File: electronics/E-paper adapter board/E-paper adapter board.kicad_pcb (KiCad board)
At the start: 2 copper layers, 50.8 x 49.7 mm, 9 parts, among them J1 EXTRA, J2 SWD, J3 J-LINK, J4 nRF-PPK2, J5 DEBUG

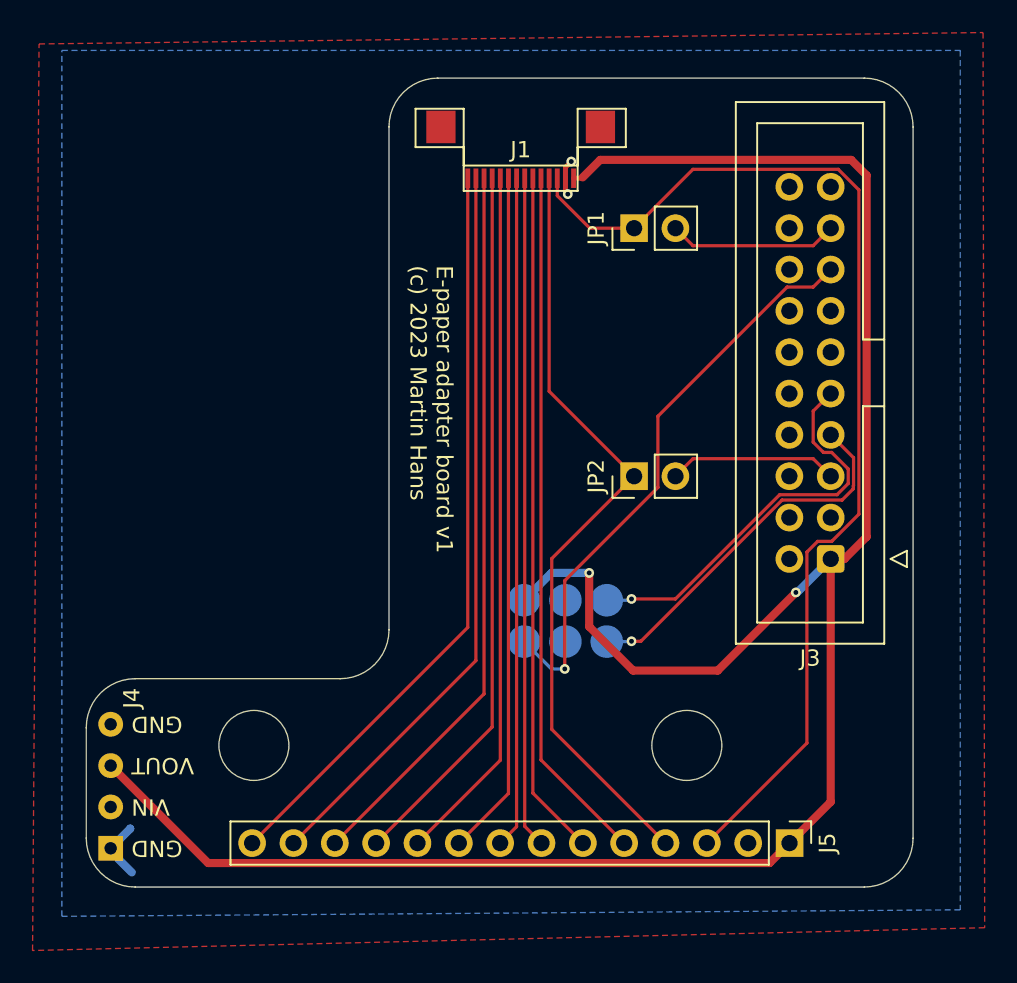
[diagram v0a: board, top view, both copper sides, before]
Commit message: fix TP4056 footprint
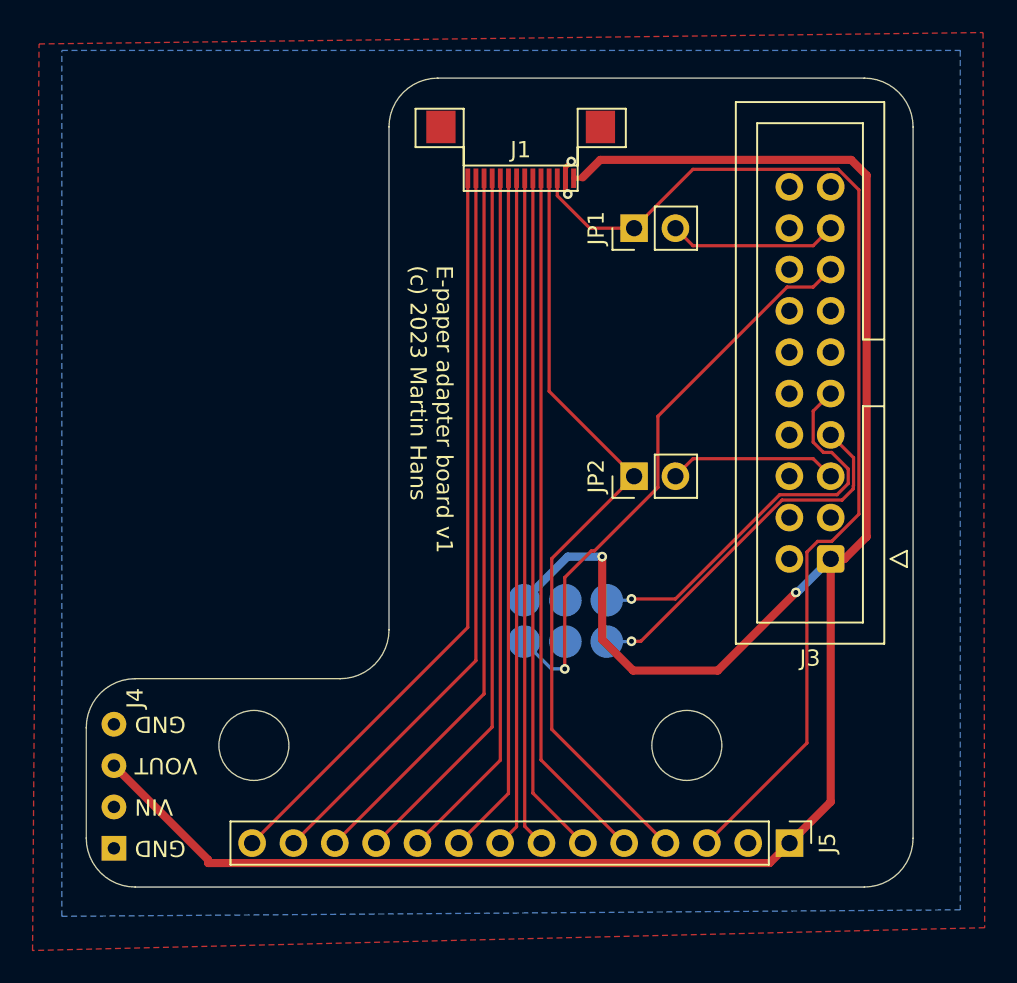
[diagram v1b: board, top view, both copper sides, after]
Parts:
- moved J4 0.20 mm to (114.5, 147.3)
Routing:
- net GND: track 5.95 -> 2.39 mm
- net +3V0: track 133.8 -> 135.6 mm
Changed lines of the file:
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@@
     (property "ki_description" "Mounting Hole without connection")
     (property "ki_keywords" "mounting hole")
-    (attr exclude_from_pos_files)
+    (attr exclude_from_pos_files exclude_from_bom)
     (fp_text reference "H2" (at 0 -4.75) (layer "F.SilkS") hide
         (effects (font (size 1 1) (thickness 0.15)))
@@
   )
   (footprint "project:nRF-PPK2_power" (layer "F.Cu")
-    (at 114.3 147.32 90)
+    (at 114.5 147.32 90)
     (property "Config" "+ci")
     (property "LCSC" "C2897386")
@@
     (property "ki_description" "Mounting Hole without connection")
     (property "ki_keywords" "mounting hole")
-    (attr exclude_from_pos_files)
+    (attr exclude_from_pos_files exclude_from_bom)
     (fp_text reference "H1" (at 0 -4.75) (layer "F.SilkS") hide
         (effects (font (size 1 1) (thickness 0.15)))
@@
     (property "ki_description" "Generic connector, double row, 02x03, counter clockwise pin numbering scheme (similar to DIP package numbering), script generated (kicad-library-utils/schlib/autogen/connector/)")
     (property "ki_keywords" "connector")
-    (attr smd exclude_from_bom)
+    (attr smd exclude_from_pos_files exclude_from_bom)
     (fp_text reference "J2" (at 0 3.81 unlocked) (layer "B.SilkS")
         (effects (font (size 1 1) (thickness 0.15)) (justify mirror))
@@
   )
   (segment (start 142.74 106.15) (end 143.25 106.15) (width 0.3) (layer "F.Cu") (net 1))
-  (segment (start 143.7 133.7) (end 146.4 136.4) (width 0.5) (layer "F.Cu") (net 1))
   (segment (start 120.287 148.227) (end 154.783 148.227) (width 0.5) (layer "F.Cu") (net 1))
+  (segment (start 120.287 148.027) (end 114.5 142.24) (width 0.5) (layer "F.Cu") (net 1))
+  (segment (start 146.4 136.4) (end 144.5 134.5) (width 0.5) (layer "F.Cu") (net 1))
   (segment (start 160.748 105.97342) (end 160.748 128.182) (width 0.5) (layer "F.Cu") (net 1))
   (segment (start 144.377 105.023) (end 159.79758 105.023) (width 0.5) (layer "F.Cu") (net 1))
-  (segment (start 146.4 136.4) (end 151.6 136.4) (width 0.5) (layer "F.Cu") (net 1))
   (segment (start 158.54 144.47) (end 156.01 147) (width 0.5) (layer "F.Cu") (net 1))
-  (segment (start 151.6 136.4) (end 156.4 131.6) (width 0.5) (layer "F.Cu") (net 1))
   (segment (start 143.25 106.15) (end 143.3 106.1) (width 0.3) (layer "F.Cu") (net 1))
   (segment (start 160.748 128.182) (end 159.39 129.54) (width 0.5) (layer "F.Cu") (net 1))
   (segment (start 159.39 129.54) (end 158.54 129.54) (width 0.5) (layer "F.Cu") (net 1))
-  (segment (start 114.3 142.24) (end 120.287 148.227) (width 0.5) (layer "F.Cu") (net 1))
-  (segment (start 143.7 130.4) (end 143.7 133.7) (width 0.5) (layer "F.Cu") (net 1))
+  (segment (start 156.4 131.6) (end 151.6 136.4) (width 0.5) (layer "F.Cu") (net 1))
   (segment (start 159.79758 105.023) (end 160.748 105.97342) (width 0.5) (layer "F.Cu") (net 1))
   (segment (start 143.3 106.1) (end 144.377 105.023) (width 0.5) (layer "F.Cu") (net 1))
   (segment (start 158.54 129.54) (end 158.54 144.47) (width 0.5) (layer "F.Cu") (net 1))
+  (segment (start 120.287 148.227) (end 120.287 148.027) (width 0.5) (layer "F.Cu") (net 1))
+  (segment (start 144.5 134.5) (end 144.5 129.4) (width 0.5) (layer "F.Cu") (net 1))
+  (segment (start 151.6 136.4) (end 146.4 136.4) (width 0.5) (layer "F.Cu") (net 1))
   (segment (start 154.783 148.227) (end 156.01 147) (width 0.5) (layer "F.Cu") (net 1))
   (via (at 156.4 131.6) (size 0.6) (drill 0.3) (layers "F.Cu" "B.Cu") (net 1))
-  (via (at 143.7 130.4) (size 0.6) (drill 0.3) (layers "F.Cu" "B.Cu") (net 1))
-  (segment (start 141.38 130.4) (end 143.7 130.4) (width 0.5) (layer "B.Cu") (net 1))
+  (via (at 144.5 129.4) (size 0.6) (drill 0.3) (layers "F.Cu" "B.Cu") (net 1))
   (segment (start 156.48 131.6) (end 158.54 129.54) (width 0.5) (layer "B.Cu") (net 1))
-  (segment (start 139.7 132.08) (end 141.38 130.4) (width 0.5) (layer "B.Cu") (net 1))
+  (segment (start 139.7 132.08) (end 142.38 129.4) (width 0.5) (layer "B.Cu") (net 1))
+  (segment (start 142.38 129.4) (end 144.5 129.4) (width 0.5) (layer "B.Cu") (net 1))
   (segment (start 156.4 131.6) (end 156.48 131.6) (width 0.5) (layer "B.Cu") (net 1))
   (segment (start 142.24 105.483498) (end 142.6 105.123498) (width 0.3) (layer "F.Cu") (net 2))
@@
   (via (at 142.38652 107.124832) (size 0.6) (drill 0.3) (layers "F.Cu" "B.Cu") (net 2))
   (via (at 142.6 105.123498) (size 0.6) (drill 0.3) (layers "F.Cu" "B.Cu") (net 2))
-  (segment (start 114.3 147.5) (end 115.6 148.8) (width 0.5) (layer "B.Cu") (net 2))
   (segment (start 114.3 147.32) (end 114.3 147.5) (width 0.5) (layer "B.Cu") (net 2))
-  (segment (start 115.5 146.1) (end 115.5 146.12) (width 0.5) (layer "B.Cu") (net 2))
-  (segment (start 114.3 147.32) (end 115.5 146.12) (width 0.5) (layer "B.Cu") (net 2))
   (segment (start 157.077 140.853) (end 150.93 147) (width 0.2) (layer "F.Cu") (net 3))
   (segment (start 146.46 109.22) (end 150.077 105.603) (width 0.2) (layer "F.Cu") (net 3))
@@
   (segment (start 146.28 134.62) (end 146.3 134.6) (width 0.2) (layer "B.Cu") (net 16))
   (segment (start 147.923 120.777) (end 155.863 112.837) (width 0.2) (layer "F.Cu") (net 18))
-  (segment (start 142.2 130.874) (end 147.923 125.151) (width 0.2) (layer "F.Cu") (net 18))
+  (segment (start 143.830761 129.05) (end 144.024 129.05) (width 0.2) (layer "F.Cu") (net 18))
   (segment (start 147.923 125.151) (end 147.923 120.777) (width 0.2) (layer "F.Cu") (net 18))
-  (segment (start 142.2 136.3) (end 142.2 130.874) (width 0.2) (layer "F.Cu") (net 18))
+  (segment (start 144.024 129.05) (end 147.923 125.151) (width 0.2) (layer "F.Cu") (net 18))
+  (segment (start 142.2 136.3) (end 142.2 130.680761) (width 0.2) (layer "F.Cu") (net 18))
+  (segment (start 142.2 130.680761) (end 143.830761 129.05) (width 0.2) (layer "F.Cu") (net 18))
+  (segment (start 155.863 112.837) (end 157.463 112.837) (width 0.2) (layer "F.Cu") (net 18))
   (segment (start 157.463 112.837) (end 158.54 111.76) (width 0.2) (layer "F.Cu") (net 18))
-  (segment (start 155.863 112.837) (end 157.463 112.837) (width 0.2) (layer "F.Cu") (net 18))
   (via (at 142.2 136.3) (size 0.6) (drill 0.3) (layers "F.Cu" "B.Cu") (net 18))
   (segment (start 141.38 136.3) (end 142.2 136.3) (width 0.2) (layer "B.Cu") (net 18))
